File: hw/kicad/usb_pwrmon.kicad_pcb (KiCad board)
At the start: 2 copper layers, 14 x 15.2 mm, 12 parts, among them P1 VLD+, P2 VBUS, P3 VOUT, P4 VLD-, P8 GND, U1 AD8591

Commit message: - fix it all up. ready to roll.
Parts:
- removed R5: R, SM0603
- added P5: SHTDN, TEST_0.100, F.Cu at (217.9, 111.6)
- P1: value VLD+ -> VLOAD+
- P3: value VOUT -> ADC_IN
- P4: value VLD- -> VLOAD-
- U1: value AD8591 -> MAX9636; footprint SOT23_6 -> MAX9636
- moved P8 6.03 mm to (215.1, 111.6)
- moved P2 2.22 mm to (220.8, 111.6)
- moved R2 1.42 mm to (215.5, 105.4)
- moved R3 0.76 mm to (215.5, 109.2)
- moved U1 0.64 mm to (219.5, 106.7), turned to 270 degrees
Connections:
- R1 pad 4: VLOAD_MEAS -> N-000007
- R2 pad 2: N-000008 -> N-000004
- R3 pad 1: N-000008 -> N-000004
- U1 pad 1: ADC_SNS_1 -> N-000007
- U1 pad 3: VLOAD_MEAS -> N-000004
- U1 pad 4: N-000008 -> ADC_SNS_1
- U1 pad 5: N-000005 -> SHTDN
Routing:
- net N-000008: track 7.83 -> 0.00 mm, vias 2 -> 0
- net N-000004: track 0.00 -> 7.49 mm
- net GND: track 2.16 -> 6.93 mm
- net SHTDN: track 0.00 -> 3.68 mm
- net VBUS: track 6.83 -> 3.34 mm, vias 2 -> 0
- net N-000007: track 0.00 -> 3.28 mm
- net N-000005: track 2.54 -> 0.00 mm
- net VLOAD_MEAS: track 1.40 -> 0.00 mm
- net ADC_SNS_1: track 13.2 -> 13.4 mm, vias 0 -> 2
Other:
- board text added: "shunt tst brd git.io/oB40EQ v0. oct-2013"
- board text removed: "shunt tst brd git.io/oB40EQ v0.1 aug-2013"

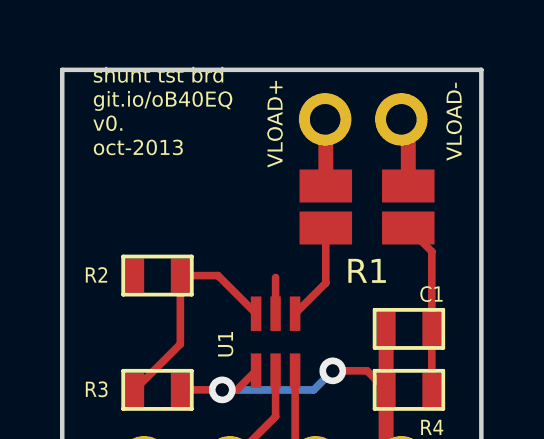
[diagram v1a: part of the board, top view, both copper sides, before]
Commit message: - fix version #, add schematic pdf
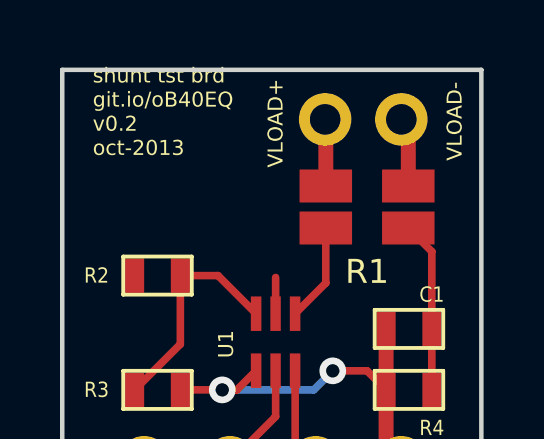
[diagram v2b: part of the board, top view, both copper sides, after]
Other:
- board text added: "shunt tst brd git.io/oB40EQ v0.2 oct-2013"
- board text removed: "shunt tst brd git.io/oB40EQ v0. oct-2013"
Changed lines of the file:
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@@
     )
   )
-  (gr_text "shunt tst brd\ngit.io/oB40EQ\nv0.\noct-2013" (at 213.36 99.949) (layer F.SilkS)
+  (gr_text "shunt tst brd\ngit.io/oB40EQ\nv0.2\noct-2013" (at 213.36 99.949) (layer F.SilkS)
     (effects (font (size 0.5 0.5) (thickness 0.125)) (justify left))
   )

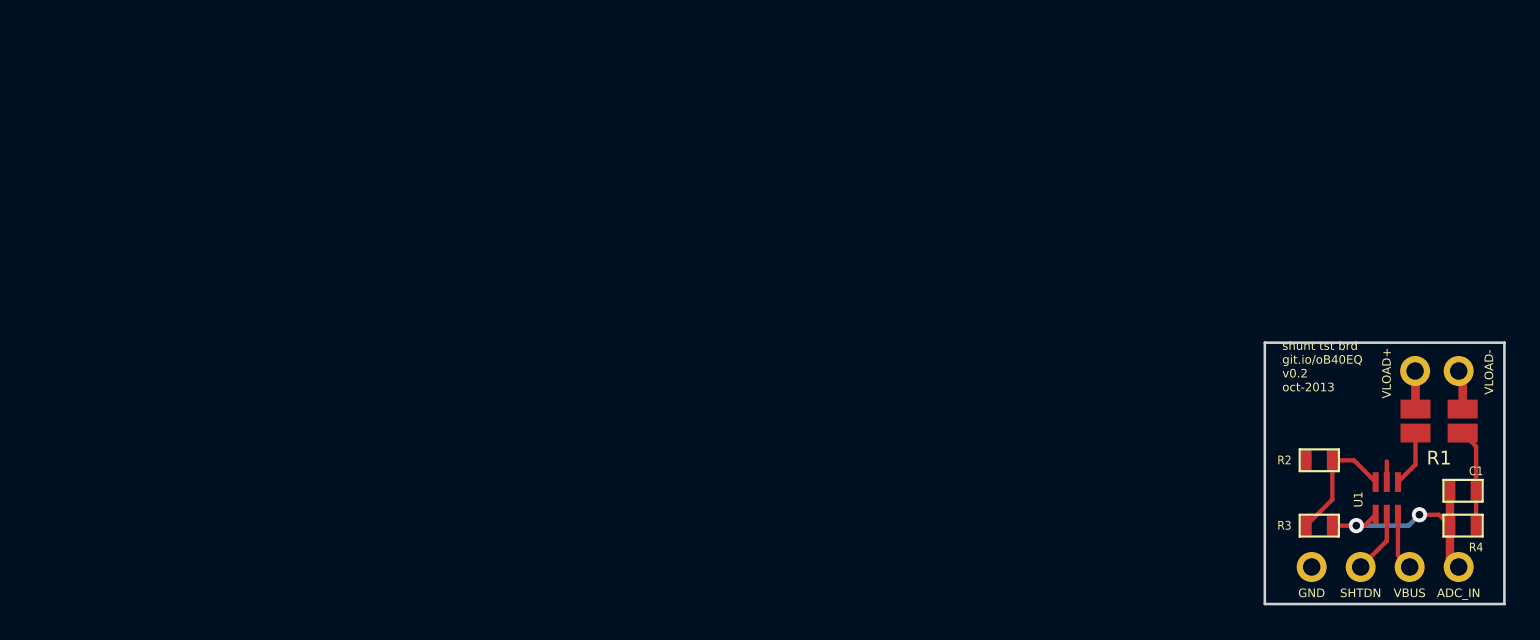
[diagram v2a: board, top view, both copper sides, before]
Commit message: - start work on pcb
Former-commit-id: 46d673d80cc2a86cb1cf0198eab2f83ad6e8f989 [formerly 46d673d80cc2a86cb1cf0198eab2f83ad6e8f989 [formerly e6562ca754a2c3bdfaa1edcaa4f370bf0480df17]]
Former-commit-id: 53930e6f4d9856f6407d59fe0fb9abf5292b8064
Former-commit-id: 7281a321fa1d9912715cdb41e797318617110904
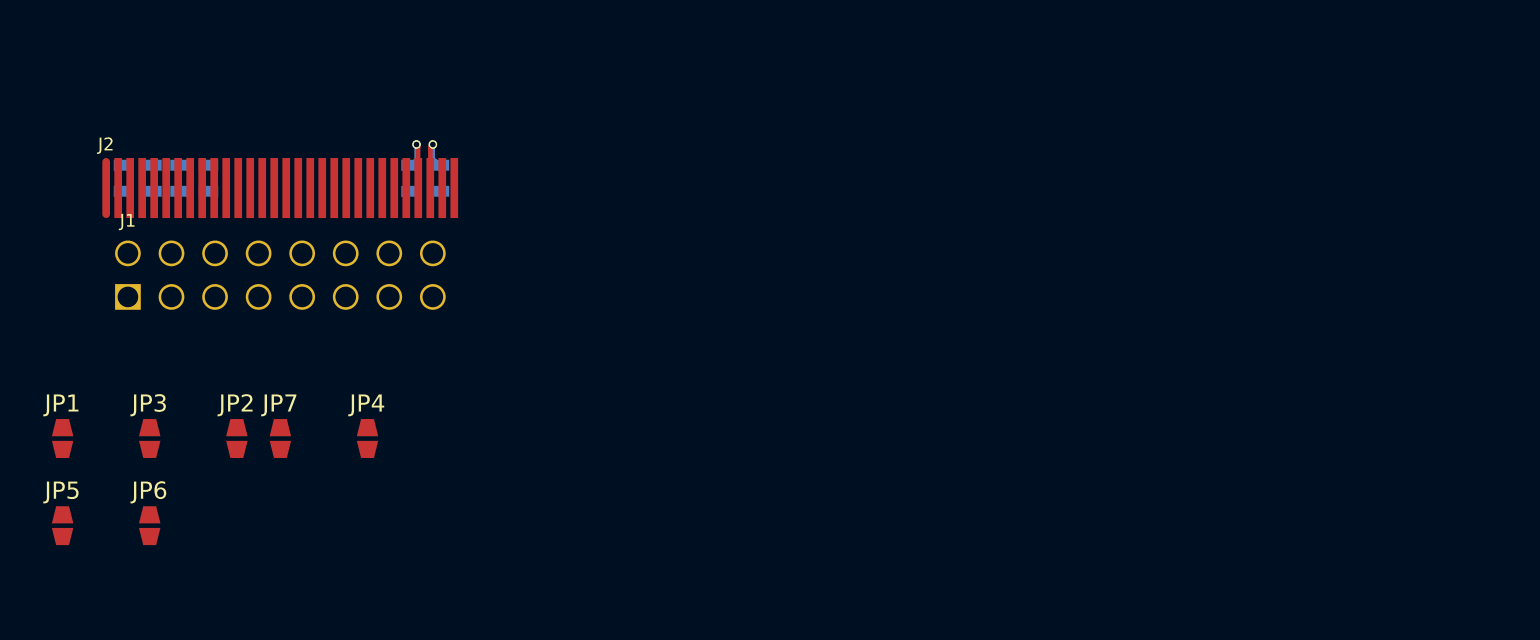
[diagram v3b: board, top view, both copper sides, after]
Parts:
- removed P1: VLOAD+, TEST_0.100
- removed P2: VBUS, TEST_0.100
- removed P3: ADC_IN, TEST_0.100
- removed P4: VLOAD-, TEST_0.100
- removed P5: SHTDN, TEST_0.100
- removed P8: GND, TEST_0.100
- removed R1: LVK12-SHUNT, lvk12
- removed R2, R3, R4: R, SM0603
- removed U1: MAX9636, MAX9636
- added C2: 1uF, SM0603, B.Cu at (145.8, 89.0)
- added C3: 1uF, SM0603, B.Cu at (147.4, 89.0)
- added C4: 1uF, SM0603, B.Cu at (149.1, 89.0)
- added C5: 1uF, SM0603, B.Cu at (150.7, 89.0)
- added C6: 10uF, SM0603, B.Cu at (164.2, 89.0)
- added J1: 16_PIN_HDR, 16_pin_double, F.Cu at (146.1, 95.9)
- added J2: OLED_FPC_CONN, oled_fpc_30, F.Cu at (144.8, 89.5)
- added JP1: JUMPER, jmp_small, F.Cu at (142.2, 104.1)
- added JP2: JUMPER, jmp_small, F.Cu at (152.4, 104.1)
- added JP3: JUMPER, jmp_small, F.Cu at (147.3, 104.1)
- added JP4: JUMPER, jmp_small, F.Cu at (160.0, 104.1)
- added JP5: JUMPER, jmp_small, F.Cu at (142.2, 109.2)
- added JP6: JUMPER, jmp_small, F.Cu at (147.3, 109.2)
- added JP7: JUMPER, jmp_small, F.Cu at (154.9, 104.1)
- C1: value C -> 2.2uF/16V; moved to B.Cu
- moved C1 64.0 mm to (162.6, 89.0), turned to 90 degrees
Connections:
- C1 pad 1: ADC_SNS_1 -> GND
- C1 pad 2: GND -> N-000003
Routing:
- net ADC_SNS_1: track 13.4 -> 0.00 mm, vias 2 -> 0
- net GND: track 6.93 -> 0.00 mm
- net N-000003: track 0.00 -> 3.92 mm, vias 0 -> 1
- net SHTDN: track 3.68 -> 0.00 mm
- net N-000004: track 7.49 -> 3.97 mm, vias 0 -> 1
- net VBUS: track 3.34 -> 0.00 mm
- net N-000007: track 3.28 -> 0.00 mm
- net VLOAD-: track 2.32 -> 0.00 mm
- net VLOAD+: track 2.23 -> 0.00 mm
- removed copper zone on B.Cu, net GND
- removed copper zone on F.Cu, net GND
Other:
- board outline removed
- net class small added: clearance 0.1524, trace_width 0.1524, via_dia 0.508, via_drill 0.33
- rule trace_min: 0.254 -> 0.1524
- rule via_min_drill: 0.508 -> 0.33
- rule via_min_size: 0.889 -> 0.508
- board text removed: "shunt tst brd git.io/oB40EQ v0.2 oct-2013"

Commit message: - some work on pcb
Former-commit-id: e83c8b7e5bcab94e8fbee646e86a45bac6c6c272 [formerly e83c8b7e5bcab94e8fbee646e86a45bac6c6c272 [formerly 18d4f19c09207a9ca7ec5a495ebeb30e648c26b6]]
Former-commit-id: 0d1dc90981a9c6c5f6a80205f9128b3a8f60f3f5
Former-commit-id: cb8426d24d42cf8ed3e902c07038b48ca8d503ca
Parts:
- JP7: moved to B.Cu
- moved JP7 15.4 mm to (157.7, 89.0)
- moved C1 0.63 mm to (162.6, 88.3)
- moved C2 0.63 mm to (145.8, 88.3)
- moved C3 0.63 mm to (147.4, 88.3)
- moved C4 0.63 mm to (149.1, 88.3)
- moved C5 0.63 mm to (150.7, 88.3)
- moved C6 0.63 mm to (164.2, 88.3)
- moved J2 0.51 mm to (144.8, 89.0)
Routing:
- net D4: track 0.00 -> 8.79 mm
- net +3.3: track 0.00 -> 7.91 mm
- net D6: track 0.00 -> 7.89 mm
- net D2/I2C_SDA: track 0.00 -> 6.85 mm
- net D3: track 0.00 -> 5.90 mm
- net D5: track 0.00 -> 5.04 mm
- net D7: track 0.00 -> 4.98 mm
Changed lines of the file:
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@@
   (general
     (links 46)
-    (no_connects 41)
-    (area 0 0 0 0)
+    (no_connects 37)
+    (area 138.577667 85.841 167.098405 111.949)
     (thickness 1.6)
     (drawings 0)
-    (tracks 10)
+    (tracks 45)
     (zones 0)
     (modules 15)
@@
   )
   (module SM0603 (layer B.Cu)
-    (at 145.796 88.9635 270)
+    (at 145.796 88.3285 270)
     (attr smd)
     (fp_text reference C2 (at 0 0 270) (layer B.SilkS)
@@
   )
   (module SM0603 (layer B.Cu)
-    (at 147.447 88.9635 90)
+    (at 147.447 88.3285 90)
     (attr smd)
     (fp_text reference C3 (at 0 0 90) (layer B.SilkS)
@@
   )
   (module SM0603 (layer B.Cu)
-    (at 149.098 88.9635 270)
+    (at 149.098 88.3285 270)
     (attr smd)
     (fp_text reference C4 (at 0 0 270) (layer B.SilkS)
@@
   )
   (module SM0603 (layer B.Cu)
-    (at 150.749 88.9635 270)
+    (at 150.749 88.3285 270)
     (attr smd)
     (fp_text reference C5 (at 0 0 270) (layer B.SilkS)
@@
   )
   (module SM0603 (layer B.Cu)
-    (at 162.56 88.9635 90)
+    (at 162.56 88.3285 90)
     (attr smd)
     (fp_text reference C1 (at 0 0 90) (layer B.SilkS)
@@
   )
   (module SM0603 (layer B.Cu)
-    (at 164.211 88.9635 90)
+    (at 164.211 88.3285 90)
     (attr smd)
     (fp_text reference C6 (at 0 0 90) (layer B.SilkS)
@@
   )
   (module oled_fpc_30 (layer F.Cu)
-    (at 144.78 89.535)
-    (fp_text reference J2 (at 0 -2.54) (layer F.SilkS)
+    (at 144.78 89.027)
+    (fp_text reference J2 (at 0 -2.54) (layer F.SilkS) hide
       (effects (font (size 0.75 0.75) (thickness 0.13)))
     )
@@
     )
   )
-  (module jmp_small (layer F.Cu)
-    (at 154.94 104.14)
-    (fp_text reference JP7 (at 0 -2.032) (layer F.SilkS)
-      (effects (font (size 1 1) (thickness 0.15)))
-    )
-    (fp_text value JUMPER (at 0 1.9) (layer F.SilkS) hide
-      (effects (font (size 1 1) (thickness 0.15)))
-    )
-    (pad 1 smd trapezoid (at 0 -0.635) (size 1 1) (rect_delta 0 0.25 )
-      (layers F.Cu F.Paste F.Mask)
+  (module jmp_small (layer B.Cu)
+    (at 157.734 89.027)
+    (fp_text reference JP7 (at 0 2.032) (layer B.SilkS)
+      (effects (font (size 0.75 0.75) (thickness 0.13)) (justify mirror))
+    )
+    (fp_text value JUMPER (at 0 -1.9) (layer B.SilkS) hide
+      (effects (font (size 1 1) (thickness 0.15)) (justify mirror))
+    )
+    (pad 1 smd trapezoid (at 0 0.635) (size 1 1) (rect_delta 0 -0.25 )
+      (layers B.Cu B.Paste B.Mask)
       (net 7 D2/I2C_SDA)
     )
-    (pad 2 smd trapezoid (at 0 0.635) (size 1 1) (rect_delta 0 -0.25 )
-      (layers F.Cu F.Paste F.Mask)
+    (pad 2 smd trapezoid (at 0 -0.635) (size 1 1) (rect_delta 0 0.25 )
+      (layers B.Cu B.Paste B.Mask)
       (net 6 D1/SPI_SDIN/I2C_SDA)
     )
@@
   (module 16_pin_double (layer F.Cu)
     (at 146.05 95.885)
-    (fp_text reference J1 (at 0 -4.445) (layer F.SilkS)
+    (fp_text reference J1 (at 0 -4.445) (layer F.SilkS) hide
       (effects (font (size 0.75 0.75) (thickness 0.13)))
     )
@@
     )
   )
-  (segment (start 162.8775 87.884) (end 162.56 88.2015) (width 0.254) (layer B.Cu) (net 21))
-  (segment (start 162.8775 86.995) (end 162.8775 87.884) (width 0.254) (layer B.Cu) (net 21))
-  (via (at 162.8775 86.995) (size 0.508) (drill 0.33) (layers F.Cu B.Cu) (net 21))
-  (segment (start 162.98 87.0975) (end 162.8775 86.995) (width 0.254) (layer F.Cu) (net 21))
-  (segment (start 162.98 89.535) (end 162.98 87.0975) (width 0.254) (layer F.Cu) (net 21))
-  (segment (start 163.83 86.995) (end 163.83 87.8205) (width 0.254) (layer B.Cu) (net 22))
-  (segment (start 163.83 87.8205) (end 164.211 88.2015) (width 0.254) (layer B.Cu) (net 22))
-  (segment (start 163.68 89.535) (end 163.68 87.145) (width 0.254) (layer F.Cu) (net 22))
-  (via (at 163.83 86.995) (size 0.508) (drill 0.33) (layers F.Cu B.Cu) (net 22))
-  (segment (start 163.68 87.145) (end 163.83 86.995) (width 0.254) (layer F.Cu) (net 22))
+  (segment (start 147.32 91.821) (end 147.32 92.456) (width 0.254) (layer F.Cu) (net 1))
+  (segment (start 146.05 95.758) (end 147.32 94.488) (width 0.254) (layer F.Cu) (net 1))
+  (segment (start 147.32 94.488) (end 147.32 92.456) (width 0.254) (layer F.Cu) (net 1))
+  (segment (start 147.32 91.821) (end 148.28 90.861) (width 0.254) (layer F.Cu) (net 1))
+  (segment (start 148.28 88.9) (end 148.28 90.861) (width 0.254) (layer F.Cu) (net 1))
+  (segment (start 146.05 95.758) (end 146.05 95.885) (width 0.254) (layer F.Cu) (net 1))
+  (segment (start 157.48 89.916) (end 157.48 94.615) (width 0.254) (layer B.Cu) (net 7))
+  (segment (start 157.48 89.916) (end 157.734 89.662) (width 0.254) (layer B.Cu) (net 7))
+  (segment (start 156.21 95.885) (end 157.48 94.615) (width 0.254) (layer B.Cu) (net 7))
+  (segment (start 157.734 91.44) (end 156.21 92.964) (width 0.254) (layer F.Cu) (net 8))
+  (segment (start 158.78 89.027) (end 158.78 91.283) (width 0.254) (layer F.Cu) (net 8))
+  (segment (start 158.78 91.283) (end 158.623 91.44) (width 0.254) (layer F.Cu) (net 8))
+  (segment (start 157.734 91.44) (end 158.623 91.44) (width 0.254) (layer F.Cu) (net 8))
+  (segment (start 156.21 92.964) (end 156.21 93.345) (width 0.254) (layer F.Cu) (net 8))
+  (segment (start 159.48 90.837) (end 159.48 91.472) (width 0.254) (layer F.Cu) (net 9))
+  (segment (start 158.75 95.885) (end 157.48 94.615) (width 0.254) (layer F.Cu) (net 9))
+  (segment (start 159.48 90.837) (end 159.48 88.9) (width 0.254) (layer F.Cu) (net 9))
+  (segment (start 158.115 92.075) (end 158.877 92.075) (width 0.254) (layer F.Cu) (net 9))
+  (segment (start 157.48 92.71) (end 158.115 92.075) (width 0.254) (layer F.Cu) (net 9))
+  (segment (start 157.48 94.615) (end 157.48 92.71) (width 0.254) (layer F.Cu) (net 9))
+  (segment (start 159.48 91.472) (end 158.877 92.075) (width 0.254) (layer F.Cu) (net 9))
+  (segment (start 160.18 91.026) (end 160.18 91.661) (width 0.254) (layer F.Cu) (net 10))
+  (segment (start 160.18 91.661) (end 158.75 93.091) (width 0.254) (layer F.Cu) (net 10))
+  (segment (start 158.75 93.345) (end 158.75 93.091) (width 0.254) (layer F.Cu) (net 10))
+  (segment (start 160.18 91.026) (end 160.18 88.9) (width 0.254) (layer F.Cu) (net 10))
+  (segment (start 160.909 91.186) (end 160.909 91.821) (width 0.254) (layer F.Cu) (net 11))
+  (segment (start 160.02 94.615) (end 160.02 92.71) (width 0.254) (layer F.Cu) (net 11))
+  (segment (start 160.02 92.71) (end 160.909 91.821) (width 0.254) (layer F.Cu) (net 11))
+  (segment (start 160.909 91.186) (end 160.909 88.929) (width 0.254) (layer F.Cu) (net 11))
+  (segment (start 160.88 88.9) (end 160.909 88.929) (width 0.254) (layer F.Cu) (net 11))
+  (segment (start 160.02 94.615) (end 161.29 95.885) (width 0.254) (layer F.Cu) (net 11))
+  (segment (start 161.58 93.055) (end 161.58 92.42) (width 0.254) (layer F.Cu) (net 12))
+  (segment (start 161.58 92.42) (end 161.58 88.9) (width 0.254) (layer F.Cu) (net 12))
+  (segment (start 161.58 93.055) (end 161.29 93.345) (width 0.254) (layer F.Cu) (net 12))
+  (segment (start 161.29 93.345) (end 161.58 93.055) (width 0.254) (layer F.Cu) (net 12))
+  (segment (start 162.8775 87.249) (end 162.56 87.5665) (width 0.254) (layer B.Cu) (net 21))
+  (segment (start 162.8775 86.36) (end 162.8775 87.249) (width 0.254) (layer B.Cu) (net 21))
+  (via (at 162.8775 86.36) (size 0.508) (drill 0.33) (layers F.Cu B.Cu) (net 21))
+  (segment (start 162.98 86.4625) (end 162.8775 86.36) (width 0.254) (layer F.Cu) (net 21))
+  (segment (start 162.98 88.9) (end 162.98 86.4625) (width 0.254) (layer F.Cu) (net 21))
+  (segment (start 163.83 86.36) (end 163.83 87.1855) (width 0.254) (layer B.Cu) (net 22))
+  (segment (start 163.83 87.1855) (end 164.211 87.5665) (width 0.254) (layer B.Cu) (net 22))
+  (segment (start 163.68 88.9) (end 163.68 86.51) (width 0.254) (layer F.Cu) (net 22))
+  (via (at 163.83 86.36) (size 0.508) (drill 0.33) (layers F.Cu B.Cu) (net 22))
+  (segment (start 163.68 86.51) (end 163.83 86.36) (width 0.254) (layer F.Cu) (net 22))
 )

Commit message: layout done
Former-commit-id: 9c344a9a71b15ff48bda0fac1c4203cdbd4489e0 [formerly 9c344a9a71b15ff48bda0fac1c4203cdbd4489e0 [formerly e8f59ff3136515c865a4abd7ded41b9bf546da5e]]
Former-commit-id: 38cdfd79c84e7dd8fb61e084b98eec9332a8d9f5
Former-commit-id: 1b2e789e887628c82bd9e890b3a6bb7a9bc0c52a
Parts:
- removed JP1, JP2, JP3, JP4, JP5, JP6: JUMPER, jmp_small
- added 1: JUMPER, jmp_small, F.Cu at (145.2, 83.4)
- added 2: JUMPER, jmp_small, F.Cu at (147.1, 83.4)
- added 3: JUMPER, jmp_small, F.Cu at (149.5, 83.4)
- added 4: JUMPER, jmp_small, F.Cu at (151.3, 83.4)
- added 5: JUMPER, jmp_small, F.Cu at (153.2, 83.4)
- added 6: JUMPER, jmp_small, F.Cu at (155.1, 83.4)
- moved C5 0.63 mm to (151.4, 88.3)
- moved C4 0.57 mm to (149.7, 88.3)
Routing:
- net +3.3: track 7.91 -> 43.9 mm, vias 0 -> 4
- net ~RST: track 0.00 -> 18.2 mm, vias 0 -> 1
- net ~CS: track 0.00 -> 16.6 mm, vias 0 -> 1
- net GND: track 0.00 -> 16.2 mm, vias 0 -> 1
- net R/W: track 0.00 -> 15.7 mm, vias 0 -> 1
- net D1/SPI_SDIN/I2C_SDA: track 0.00 -> 12.8 mm, vias 0 -> 1
- net BS0: track 0.00 -> 10.8 mm
- net DC/I2X_SA0: track 0.00 -> 9.14 mm
- net D0/SPI_SCLK/I2C_SCK: track 0.00 -> 8.59 mm
- net BS1: track 0.00 -> 8.01 mm
- net E/RD: track 0.00 -> 8.00 mm
- net D2/I2C_SDA: track 6.85 -> 14.4 mm, vias 0 -> 1
- net BS2: track 0.00 -> 7.20 mm
- net N-0000019: track 0.00 -> 5.82 mm, vias 0 -> 1
- net N-0000017: track 0.00 -> 5.75 mm, vias 0 -> 1
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- added copper zone on B.Cu, net GND
- added copper zone on F.Cu, net GND
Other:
- board outline added: 23.9 x 17.5 mm

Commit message: as ordered
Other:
- board text added: "git.io/18upyg oled_brkout v0.1"
